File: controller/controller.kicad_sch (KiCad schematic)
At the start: 14 parts, among them SW1 SW_Push, SW2 SW_Push, SW3 SW_Push, SW4 SW_Push, U1 COM-09032, U2 COM-09032, U3 NRF24L01_Breakout

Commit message: [pcb] controller layout
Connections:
- net +3.3V: no longer U2.V1 (V+)
- net GND: no longer U2.V3 (V-)
- net JOY1_H: now also A1.32 (GPIO27_ADC1); no longer A1.14 (GPIO10)
- net JOY1_V: now also A1.31 (GPIO26_ADC0); no longer A1.12 (GPIO9)
- net JOY2_H: now also A1.34 (GPIO28_ADC2); no longer A1.16 (GPIO12)
- net NRF_CE: now also A1.12 (GPIO9); no longer A1.17 (GPIO13)
- net JOY2_V: no longer names the net of U2.V2 (V)
- net JOY2_V: no longer A1.15 (GPIO11)
- no-connect marks 14 -> 17

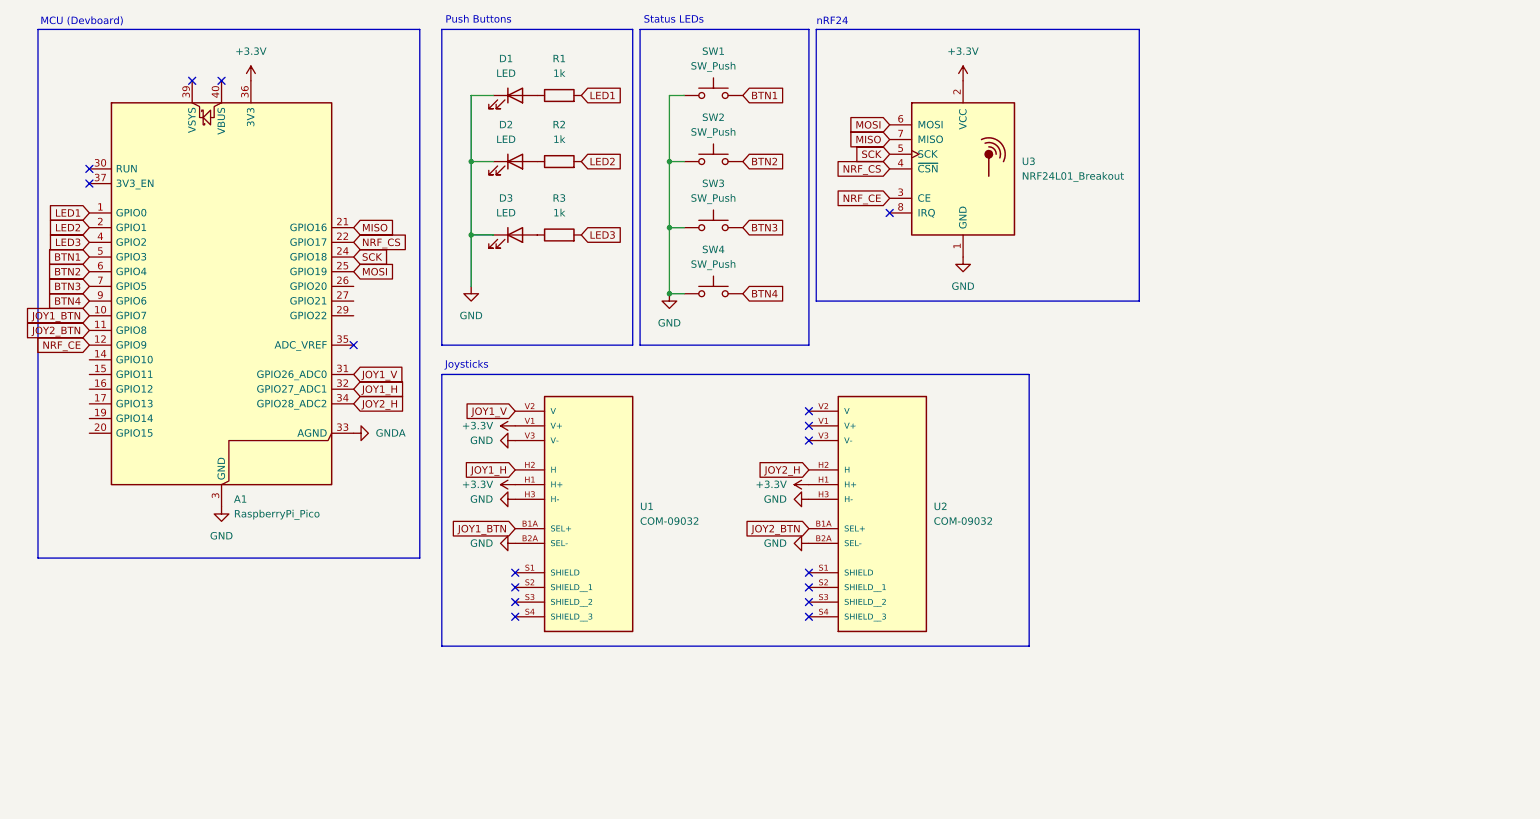
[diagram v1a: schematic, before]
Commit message: [pcb] change pico for c3 supermini and use priority encoder for more inputs
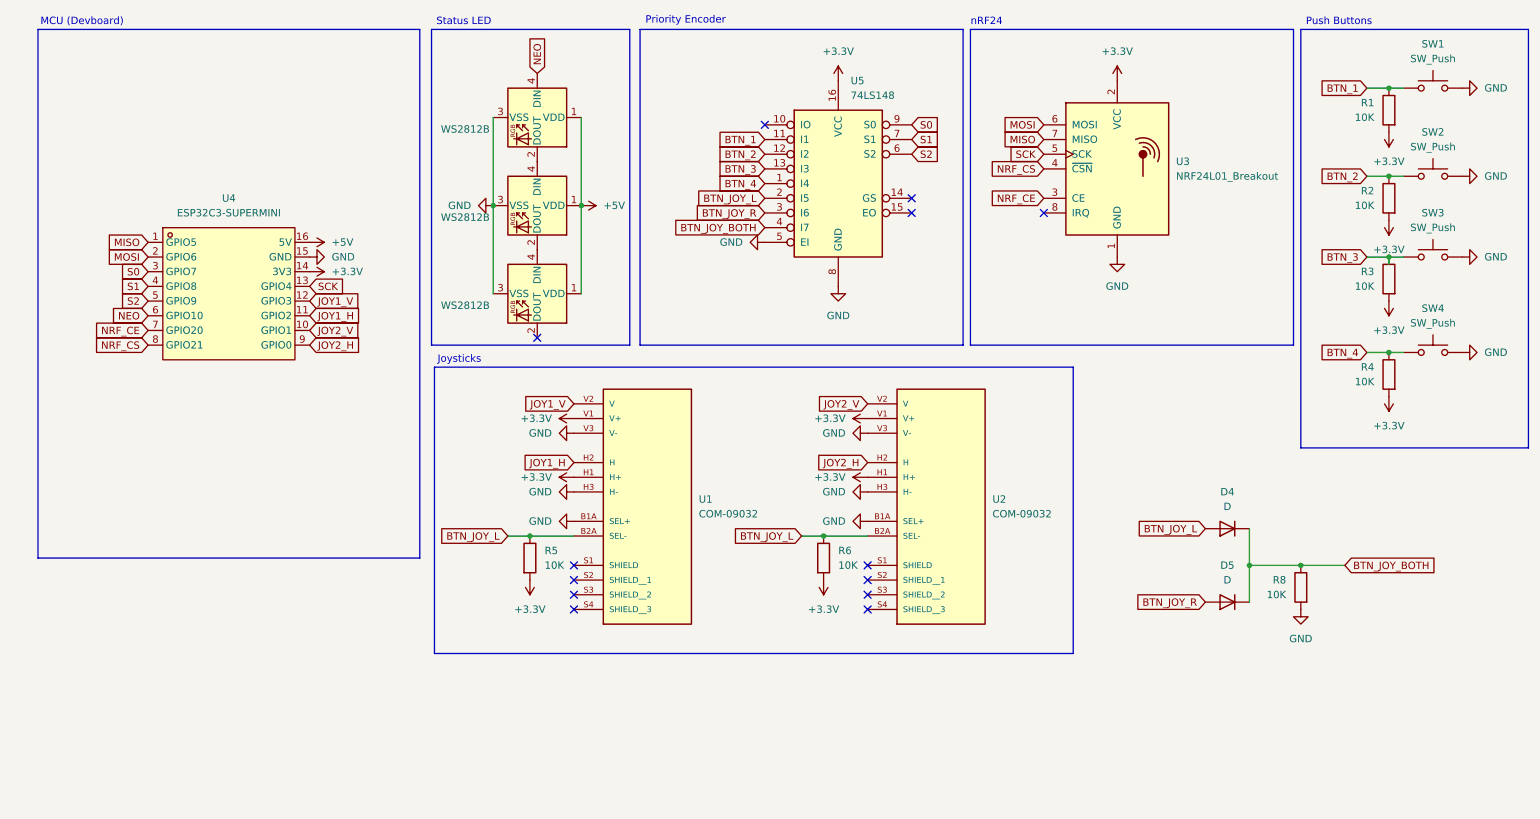
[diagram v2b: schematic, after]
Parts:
- removed A1: RaspberryPi_Pico, Module:RaspberryPi_Pico_Common_Unspecified, symbol MCU_Module:RaspberryPi_Pico
- removed D1, D2, D3: LED, LED_THT:LED_D5.0mm, symbol Device:LED
- added D1, D2, D3: WS2812B, LED_SMD:LED_WS2812B_PLCC4_5.0x5.0mm_P3.2mm, symbol LED:WS2812B
- added D4, D5: D, symbol Device:D
- added R4, R5, R6, R8: 10K, symbol Device:R
- added U4: ESP32C3-SUPERMINI, stuff:COMM-SMD_16P-L22.5-W18.0-P2.54-TL, symbol stuff:ESP32C3-SUPERMINI
- added U5: 74LS148, symbol 74xx:74LS148
- R1, R2, R3: value 1k -> 10K; footprint Resistor_THT:R_Axial_DIN0204_L3.6mm_D1.6mm_P7.62mm_Horizontal -> (none)
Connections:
- net BTN1 is gone; now on net GND: SW1.2
- net BTN2 is gone; now on net GND: SW2.2
- net BTN3 is gone; now on net GND: SW3.2
- net BTN4 is gone; now on net GND: SW4.2
- net JOY1_BTN is gone; now on net GND: U1.B1A (SEL+)
- net JOY2_BTN is gone; now on net GND: U2.B1A (SEL+)
- net LED1 is gone; now on net +3.3V: R1.2
- net LED2 is gone; now on net +3.3V: R2.2
- net LED3 is gone; now on net +3.3V: R3.2
- net +3.3V: now also U2.V1 (V+), R4.2, R5.2, R6.2, U4.14 (3V3), U5.16 (VCC)
- net GND: now also U2.V3 (V-), D1.3 (VSS), D2.3 (VSS), D3.3 (VSS), R8.2, U4.15 (GND), U5.5 (EI), U5.8 (GND); no longer SW1.1, SW2.1, SW3.1, SW4.1, U1.B2A (SEL-), U2.B2A (SEL-)
- net JOY1_H: now also U4.11 (GPIO2)
- net JOY1_V: now also U4.12 (GPIO3)
- net JOY2_H: now also U4.9 (GPIO0)
- net MISO: now also U4.1 (GPIO5)
- net MOSI: now also U4.2 (GPIO6)
- net NRF_CE: now also U4.7 (GPIO20)
- net NRF_CS: now also U4.8 (GPIO21)
- net SCK: now also U4.13 (GPIO4)
- net BTN_3: now reaches R3.1
- net BTN_3: now also SW3.1, U5.13 (I3)
- net BTN_2: now reaches R2.1
- net BTN_2: now also SW2.1, U5.12 (I2)
- net BTN_1: now reaches R1.1
- net BTN_1: now also SW1.1, U5.11 (I1)
- net JOY2_V: now reaches U2.V2 (V)
- net JOY2_V: now also U4.10 (GPIO1)
- new net: D2.2 (DOUT), D3.4 (DIN)
- new net: D1.2 (DOUT), D2.4 (DIN)
- new net +5V: D1.1 (VDD), D2.1 (VDD), D3.1 (VDD), U4.16 (5V)
- new net BTN_4: R4.1, SW4.1, U5.1 (I4)
- new net BTN_JOY_BOTH: D4.1 (K), D5.1 (K), R8.1, U5.4 (I7)
- new net BTN_JOY_L: D4.2 (A), R5.1, R6.1, U1.B2A (SEL-), U2.B2A (SEL-), U5.2 (I5)
- new net BTN_JOY_R: D5.2 (A), U5.3 (I6)
- new net NEO: D1.4 (DIN), U4.6 (GPIO10)
- new net S0: U4.3 (GPIO7), U5.9 (S0)
- new net S1: U4.4 (GPIO8), U5.7 (S1)
- new net S2: U4.5 (GPIO9), U5.6 (S2)
- no-connect marks 17 -> 13
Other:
- note added: "Priority Encoder"
- note added: "Status LED"
- note removed: "Status LEDs"
- moved on the sheet: SW1, SW2, SW3, SW4, U1, U2, U3

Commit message: [pcb] finish controller schematic, route controller pcb
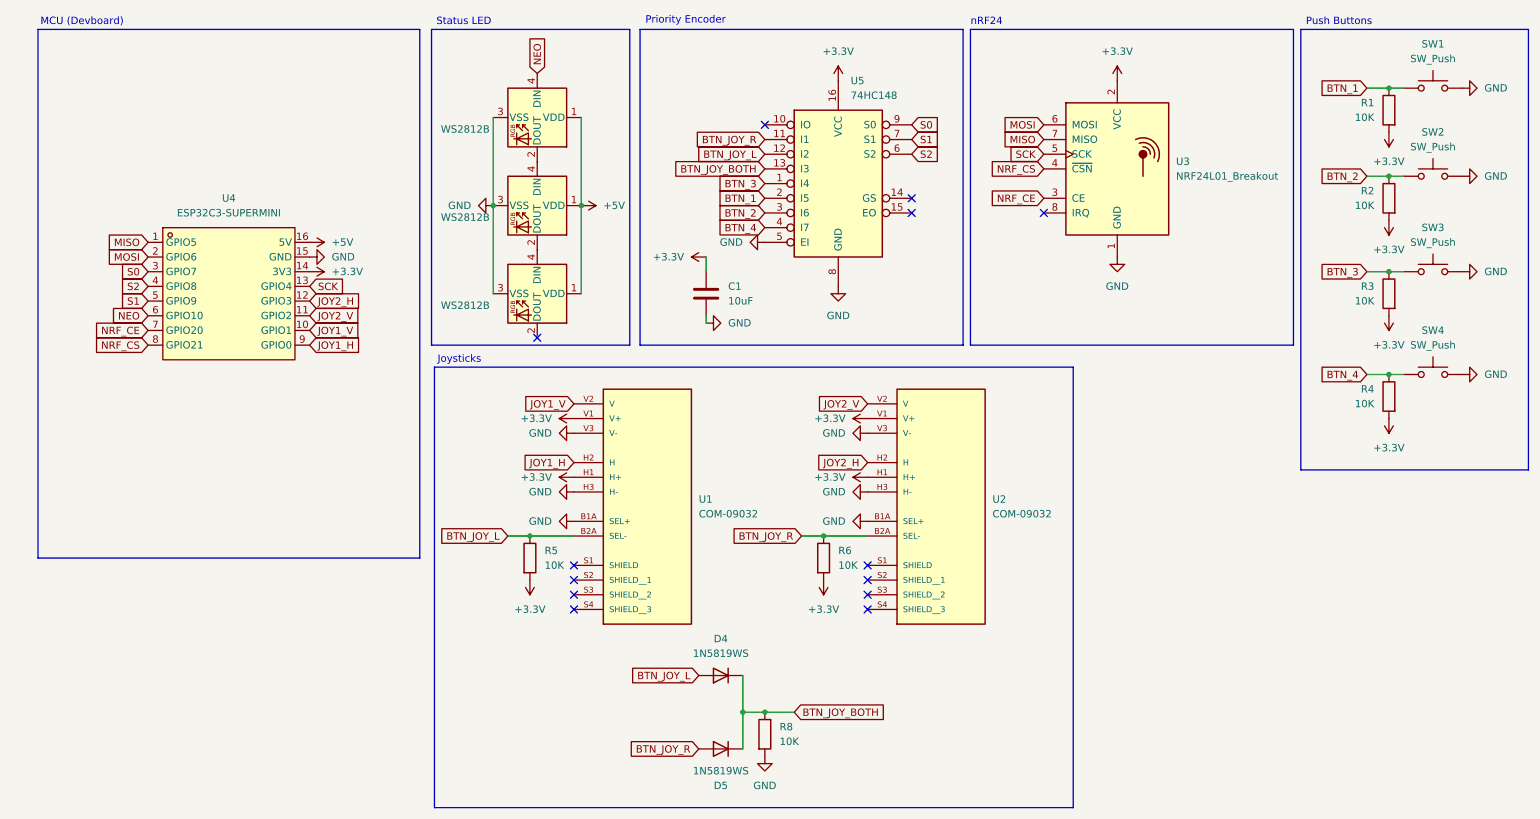
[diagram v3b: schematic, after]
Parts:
- added C1: 10uF, Capacitor_SMD:C_0805_2012Metric, symbol Device:C
- D4, D5: value D -> 1N5819WS; footprint (none) -> Diode_THT:D_DO-41_SOD81_P7.62mm_Horizontal
- R1, R2, R3, R4, R5, R6, R8: footprint (none) -> Resistor_SMD:R_0805_2012Metric
- SW1, SW2, SW3, SW4: footprint Button_Switch_THT:SW_PUSH_6mm -> Button_Switch_THT:SW_PUSH-12mm
- U4: footprint stuff:COMM-SMD_16P-L22.5-W18.0-P2.54-TL -> stuff:ESP32-C3-SuperMini
- U5: value 74LS148 -> 74HC148; footprint (none) -> Package_SO:SOP-16_3.9x9.9mm_P1.27mm
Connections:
- net +3.3V: now also C1.1
- net BTN_1: now also U5.2 (I5); no longer U5.11 (I1)
- net BTN_2: now also U5.3 (I6); no longer U5.12 (I2)
- net BTN_3: now also U5.1 (I4); no longer U5.13 (I3)
- net BTN_4: now also U5.4 (I7); no longer U5.1 (I4)
- net BTN_JOY_BOTH: now also U5.13 (I3); no longer U5.4 (I7)
- net BTN_JOY_L: now also U5.12 (I2); no longer R6.1, U2.B2A (SEL-), U5.2 (I5)
- net BTN_JOY_R: now also R6.1, U2.B2A (SEL-), U5.11 (I1); no longer U5.3 (I6)
- net GND: now also C1.2
- net JOY1_H: now also U4.9 (GPIO0); no longer U4.11 (GPIO2)
- net JOY1_V: now also U4.10 (GPIO1); no longer U4.12 (GPIO3)
- net JOY2_H: now also U4.12 (GPIO3); no longer U4.9 (GPIO0)
- net JOY2_V: now also U4.11 (GPIO2); no longer U4.10 (GPIO1)
- net S1: now also U4.5 (GPIO9); no longer U4.4 (GPIO8)
- net S2: now also U4.4 (GPIO8); no longer U4.5 (GPIO9)
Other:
- moved on the sheet: D4, D5, R3, R4, R8, SW3, SW4
